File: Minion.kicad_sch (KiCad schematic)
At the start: 63 parts, among them J1 USB_C_Receptacle_USB2.0_16P, J2 USB_A, J3 473092651, J4 PJ-320D-A, Q1 AO3401A, SW1 SW_Push, SW2 SW_Push, SW3 SW_Push, SW4 RotaryEncoder, SW5 SW_Push, SW6 SW_Push, U1 ESP32-S3-WROOM-1, U2 AMS1117-3.3, U3 FE1.1s, U4 ADXL343, U5 CH376T, U6 MCP73831-2-MC, U7 PCM5102A, Y1 12MHz, Y2 12MHz

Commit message: added bom with prices
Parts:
- U2: DigiKey (none) -> 4518-AMS1117-3.3CT-ND
- U7: DigiKey (none) -> 296-36707-1-ND; LCSC C107671 -> (none)
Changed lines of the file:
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@@
 			)
 		)
-		(property "LCSC" "C107671"
+		(property "LCSC" ""
 			(at 189.23 207.01 0)
 			(effects
@@
 			)
 		)
-		(property "DigiKey" ""
+		(property "DigiKey" "296-36707-1-ND"
 			(at 189.23 207.01 0)
 			(effects
@@
 			)
 		)
-		(property "DigiKey" ""
+		(property "DigiKey" "4518-AMS1117-3.3CT-ND"
 			(at 205.74 77.47 0)
 			(effects

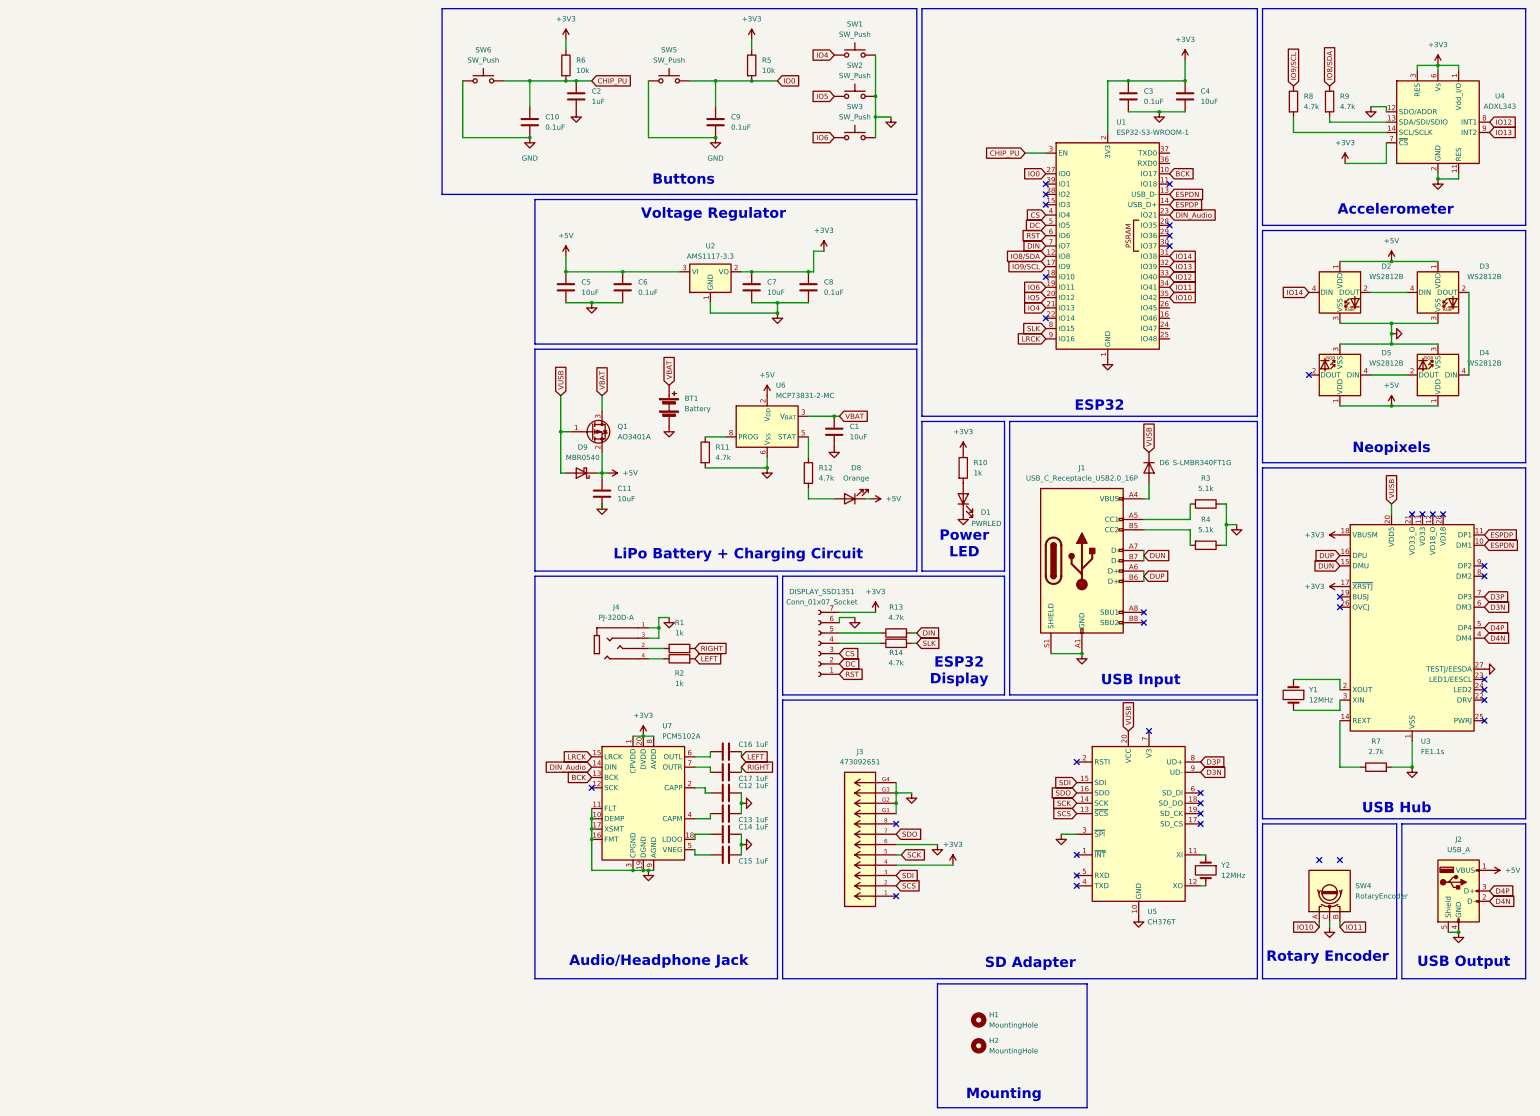
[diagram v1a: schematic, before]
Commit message: Updated from feedback
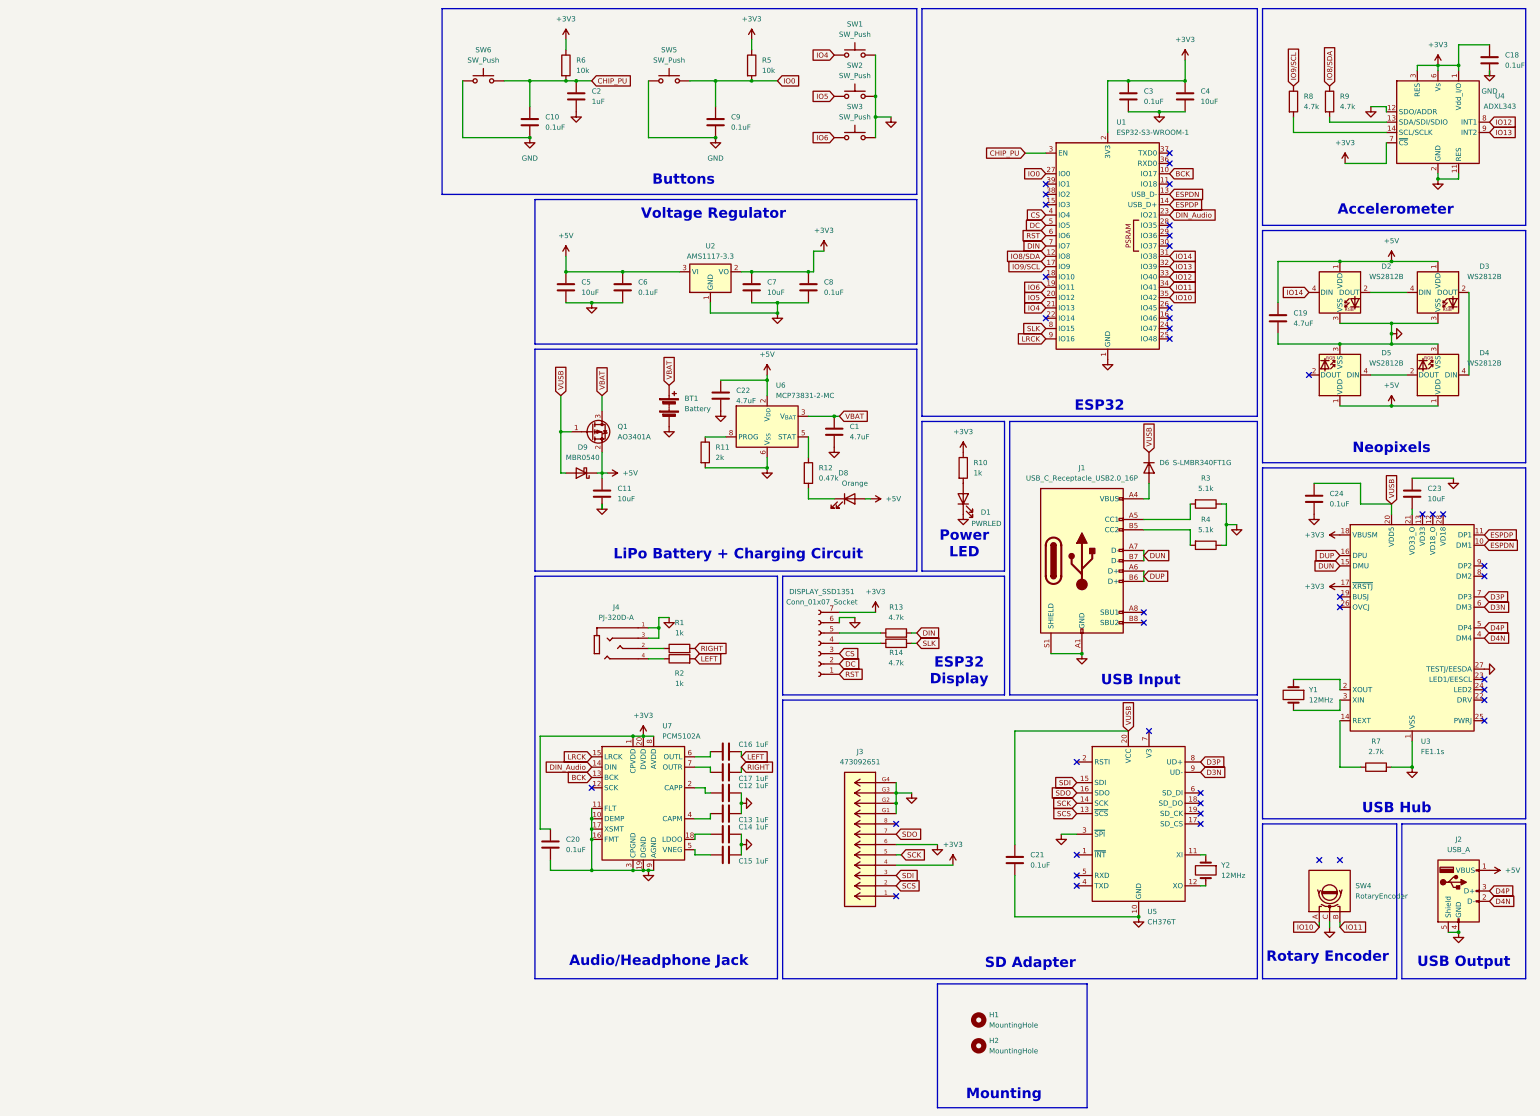
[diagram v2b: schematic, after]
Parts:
- added C18, C20, C21, C24: 0.1uF, Capacitor_SMD:C_0805_2012Metric, symbol Device:C
- added C19, C22: 4.7uF, Capacitor_SMD:C_0805_2012Metric, symbol Device:C
- added C23: 10uF, Capacitor_SMD:C_0805_2012Metric, symbol Device:C
- C1: value 10uF -> 4.7uF
- D6: footprint Diode_SMD:D_0805_2012Metric -> Diode_SMD:D_SOD-123F
- R11: value 4.7k -> 2k
- R12: value 4.7k -> 0.47k
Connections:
- net +3V3: now also C18.1, C20.1
- net +5V: now also D8.2 (A), C19.1, C22.1; no longer D8.1 (K)
- net GND: now also C18.2, C19.2, C20.2, C21.2, C22.2, C23.1, C24.2
- net VUSB: now also C21.1, C24.1
- net at U3.21 (VD33_O): now also C23.2
- net at R12.2: now also D8.1 (K); no longer D8.2 (A)
- no-connect marks 38 -> 43
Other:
- title: (none) -> Minion
- moved on the sheet: D8

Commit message: Finished PCB!
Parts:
- removed C19: 4.7uF, Capacitor_SMD:C_0805_2012Metric, symbol Device:C
- removed D2, D3, D4, D5: WS2812B, LED_SMD:LED_WS2812B_PLCC4_5.0x5.0mm_P3.2mm, symbol LED:WS2812B
- removed D6: S-LMBR340FT1G, Diode_SMD:D_SOD-123F, symbol Device:D
- removed U2: AMS1117-3.3, Package_TO_SOT_SMD:SOT-223-3_TabPin2, symbol Regulator_Linear:AMS1117-3.3
- removed U3: FE1.1s, Package_SO:SSOP-28_3.9x9.9mm_P0.635mm, symbol Interface_USB:FE1.1s
- removed U5: CH376T, Package_SO:SSOP-20_5.3x7.2mm_P0.65mm, symbol Interface:CH376T
- removed Y1, Y2: 12MHz, Crystal:Crystal_SMD_5032-2Pin_5.0x3.2mm, symbol Device:Crystal
- added C26, C29, C30, C31: 0.1uF, Capacitor_SMD:C_0805_2012Metric, symbol Device:C
- added C27, C28: 4.7uF, Capacitor_SMD:C_0805_2012Metric, symbol Device:C
- added C32, C33: 18pF, Capacitor_SMD:C_0402_1005Metric, symbol Device:C
- added R15, R16, R20: 10k, Resistor_SMD:R_0805_2012Metric, symbol Device:R
- added R17, R18, R21: 100k, Resistor_SMD:R_0805_2012Metric, symbol Device:R
- added R19: 1M, Resistor_SMD:R_0805_2012Metric, symbol Device:R
- added R22: 12k, Resistor_SMD:R_0805_2012Metric, symbol Device:R
- added U2, U3: AP2112K-3.3, Package_TO_SOT_SMD:SOT-23-5, symbol Regulator_Linear:AP2112K-3.3
- added U8: USB2641I-HZH-02, USB2641:QFN48_7X7MC_MCH, symbol 2025-06-14_17-00-00:USB2641I-HZH-02
- added Y3: 24MHz, Crystal:Crystal_SMD_5032-2Pin_5.0x3.2mm, symbol Device:Crystal
- C1, C22: LCSC C40894 -> C1779
- C10: value 0.1uF -> 10uF; LCSC C476766 -> C15850
- C11, C4, C5, C7: LCSC C40894 -> C15850
- C12, C13, C14, C15, C16, C17: LCSC C215803 -> C28323
- C18, C20, C21, C24: LCSC (none) -> C28233
- C2: value 1uF -> 10uF; LCSC C215803 -> C15850
- C23: LCSC (none) -> C15850
- C3, C6, C8, C9: LCSC C476766 -> C28233
- R1, R10, R2: LCSC C95781 -> C17513
- R11: LCSC C60816 -> C17604
- R12: LCSC C60816 -> C17710
- R13, R14, R8, R9: value 4.7k -> 4k7; LCSC C60816 -> C17673
- R3, R4: value 5.1k -> 5k1
- R5, R6: LCSC C2930231 -> C17414
- R7: value 2.7k -> 10k; LCSC C2907305 -> C17414
- renumbered DISPLAY_SSD1351 to J5
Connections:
- net +3V3: now also R13.2, R14.2, R8.1, R9.1, U7.17 (XSMT), U2.5 (VOUT); no longer J3.4
- net +5V: now also U2.1 (VIN), U2.3 (EN); no longer J2.1 (VBUS)
- net DUN: now also U8.43 (USB-)
- net DUP: now also U8.42 (USB+)
- net ESPDN: now also U8.3 (USBDN_DM3)
- net ESPDP: now also U8.4 (USBDN_DP3)
- net GND: now also C2.2, C23.2, R1.2, R2.2, U7.12 (SCK), C26.2, C27.2, C28.2, C29.2, C30.1, C31.2, C32.2, C33.2, R15.2, R16.2, R17.2, R22.2, U2.2 (GND), U3.2 (GND), U8.40 (TEST), U8.49 (EPAD); no longer C2.1, C23.1, U7.17 (XSMT)
- net LEFT: now also J4.4, R2.1; no longer R2.2
- net RIGHT: now also J4.2, R1.1; no longer R1.2
- net VUSB: now also C2.1, J1.A4 (VBUS), J1.A9 (VBUS), J1.B4 (VBUS), J1.B9 (VBUS), J2.1 (VBUS), R7.1, R18.2, U3.1 (VIN), U3.3 (EN); no longer C24.1
- net SLK_Display: now reaches J5.4 (Pin_4), R14.1
- net SLK_Display: now also U1.8 (IO15)
- net DIN_Display: now reaches J5.5 (Pin_5), R13.1
- net DIN_Display: now also U1.7 (IO7)
- net ADXL_SDA: now reaches R9.2, U4.13 (SDA/SDI/SDIO)
- net ADXL_SDA: now also U1.12 (IO8)
- net SD_D2: now reaches J3.1
- net SD_D2: now also U8.33 (SD_D2)
- net SD_D1: now reaches J3.8
- net SD_D1: now also U8.17 (SD_D1/MS_D5)
- net ADXL_SCL: now reaches R8.2, U4.14 (SCL/SCLK)
- net ADXL_SCL: now also U1.17 (IO9)
- net BCK renamed BCK_Audio
- removed net CHIP_PU: C10.1, C2.2, R6.2, SW6.2, U1.3 (EN)
- net CS renamed CS_Display
- net D4N renamed D2N
- net D2N: now also U8.1 (USBDN_DM2)
- net D4P renamed D2P
- net D2P: now also U8.2 (USBDN_DP2)
- net DC renamed DC_Display
- removed net DIN: R13.2, U1.7 (IO7)
- net IO10 renamed ROTARY_A
- net IO11 renamed ROTARY_B
- net IO12 renamed ADXL_INT1
- net IO13 renamed ADXL_INT2
- net IO14 renamed Neopixels
- net IO4 renamed BUTTON_1
- net IO5 renamed BUTTON_2
- net IO6 renamed BUTTON_3
- removed net IO8/SDA: R9.1, U1.12 (IO8)
- removed net IO9/SCL: R8.1, U1.17 (IO9)
- net LRCK renamed LRCK_Audio
- net RST renamed RST_Display
- net SCK renamed SD_CLK
- net SD_CLK: now also U8.21 (SD_CLK/MS_BS)
- net SCS renamed SD_D3
- net SD_D3: now also U8.32 (SD_D3/MS_D3)
- net SDI renamed SD_CMD
- net SD_CMD: now also U8.24 (SD_CMD/MS_D0)
- net SDO renamed SD_D0
- net SD_D0: now also U8.18 (SD_D0/MS_D4)
- removed net SLK: R14.2, U1.8 (IO15)
- new net: R17.1, R18.1, U8.39 (VBUS_DET)
- new net: R15.1, U8.14 (SD_NCD)
- new net: C30.2, U8.15 (CRFILT)
- new net: R21.1, R6.2, SW6.2
- new net: R16.1, U8.13 (SD_WP/MS_SCLK)
- new net: C33.1, R19.2, U8.44 (XTAL2), Y3.1
- new net: C32.1, R19.1, U8.45 (XTAL1(CLKIN)), Y3.2
- new net: R20.2, U8.38 (NRESET)
- new net: C31.1, U8.46 (PLLFILT)
- new net: R22.1, U8.47 (RBIAS)
- new net ESP_EN: C10.1, R21.2, U1.3 (EN)
- new net VUSB3V3: C23.1, C24.1, C26.1, C27.1, C28.1, C29.1, J3.4, R20.1, U3.5 (VOUT), U8.12 (VDD33), U8.16 (VDD33), U8.25 (VDD33), U8.34 (VDD33), U8.41 (VDD33), U8.48 (VDD33), U8.5 (VDD33)
- no-connect marks 43 -> 30
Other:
- note added: "USB2641 Hub + SD"
- note removed: "Neopixels"
- note removed: "USB Hub"
- moved on the sheet: BT1, C10, C11, C12, C13, C14, C15, C16, C17, C20, D1, J1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
